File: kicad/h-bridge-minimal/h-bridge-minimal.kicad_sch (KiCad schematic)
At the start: 28 parts, among them Q1 BC237, Q2 BC237, Q3 Q_NMOS_DGS, Q4 Q_NMOS_DGS, Q5 Q_NMOS_DGS, Q6 Q_NMOS_DGS, Q7 BC237, Q8 BC237

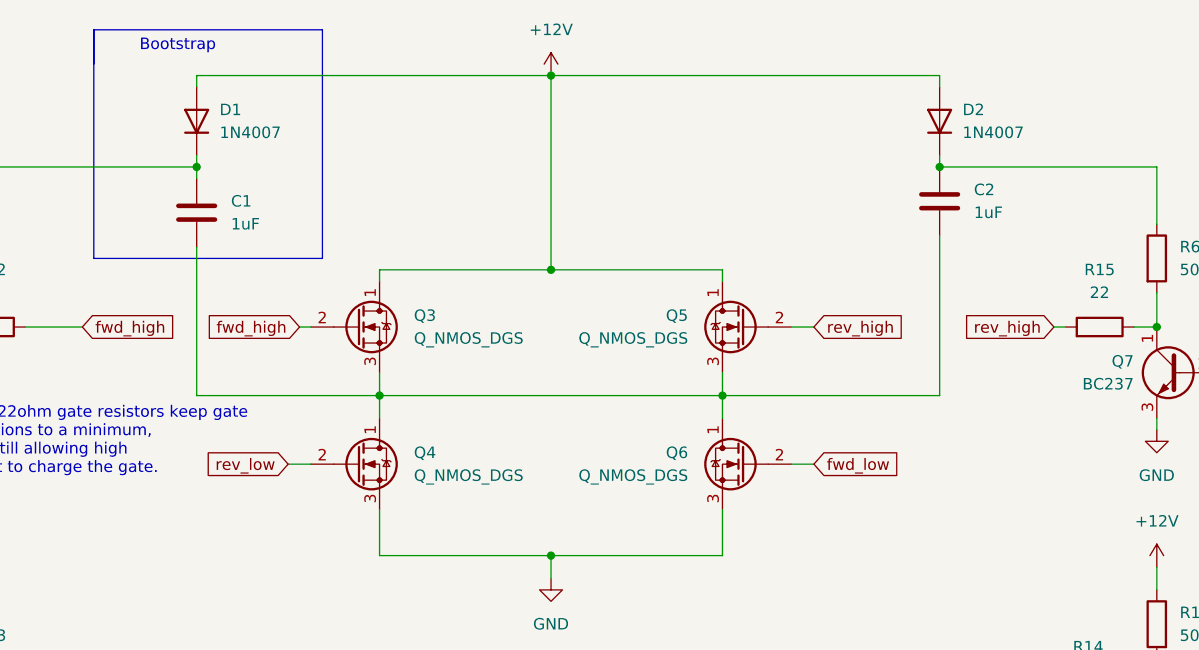
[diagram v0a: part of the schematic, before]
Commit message: Added SerialPlot class for plotting variables
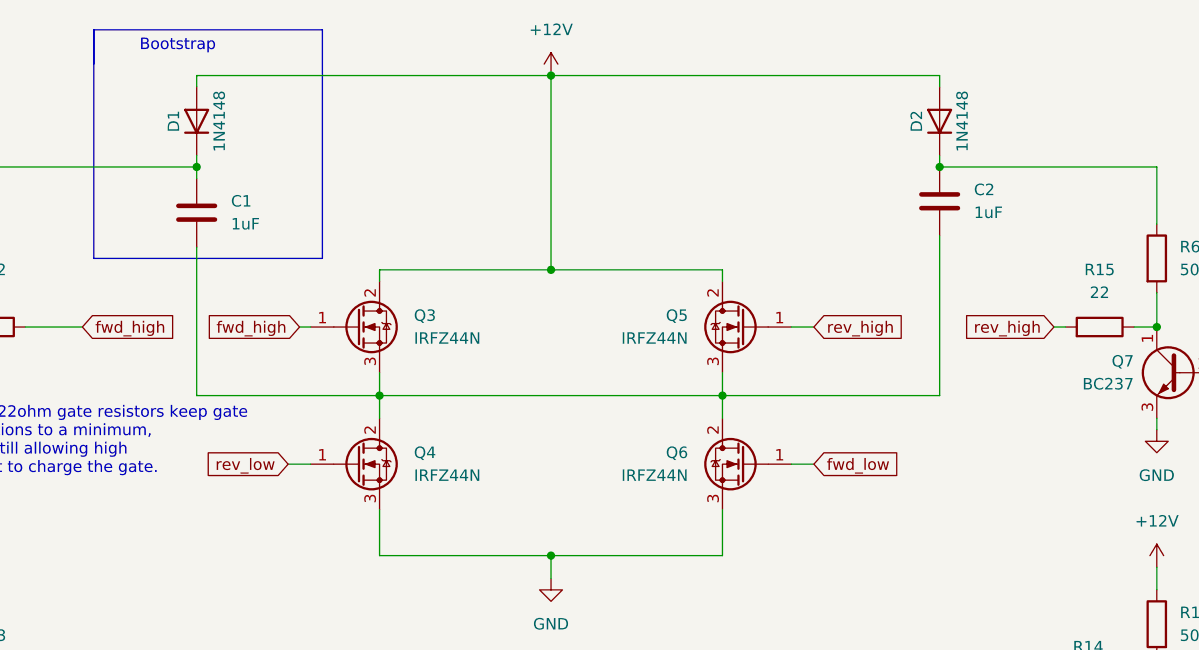
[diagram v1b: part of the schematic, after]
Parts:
- removed Q4, Q5, Q6: Q_NMOS_DGS, Package_TO_SOT_THT:TO-220-3_Vertical, symbol Device:Q_NMOS_DGS
- added Q4, Q5, Q6: IRFZ44N, Package_TO_SOT_THT:TO-220-3_Vertical, symbol Device:Q_NMOS_GDS
- C1, C2: footprint (none) -> Capacitor_THT:C_Rect_L7.2mm_W3.0mm_P5.00mm_FKS2_FKP2_MKS2_MKP2
- D1, D2: value 1N4007 -> 1N4148; footprint Diode_THT:D_DO-41_SOD81_P10.16mm_Horizontal -> Diode_THT:D_DO-35_SOD27_P7.62mm_Horizontal; symbol Diode:1N4007 -> Diode:1N4148
- Q1, Q2, Q7, Q8: footprint Package_TO_SOT_THT:TO-92_Inline -> Package_TO_SOT_THT:TO-92_Inline_Wide
- Q3: value Q_NMOS_DGS -> IRFZ44N; symbol Device:Q_NMOS_DGS -> Device:Q_NMOS_GDS
- R1, R10, R11, R12, R13, R14, R15, R16, R2, R3, R4, R5, R6, R7, R8, R9: footprint (none) -> Resistor_THT:R_Axial_DIN0207_L6.3mm_D2.5mm_P10.16mm_Horizontal
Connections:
- net +12V: now also Q3.2 (D), Q5.2 (D); no longer Q3.1 (D)
- net GND: now also Q4.3 (S), Q6.3 (S)
- net fwd_high: now also Q3.1 (G); no longer Q3.2 (G)
- net fwd_low: now also Q6.1 (G)
- net rev_high: now also Q5.1 (G)
- net rev_low: now also Q4.1 (G)
- net at C1.2, C2.2, Q3.3 (S): now also Q4.2 (D), Q5.3 (S), Q6.2 (D)
